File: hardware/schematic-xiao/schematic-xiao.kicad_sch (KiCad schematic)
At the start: 8 parts, among them SW1 SW_STD-ALN, SW2 SW_Push, U4 XIAO ESP32C3

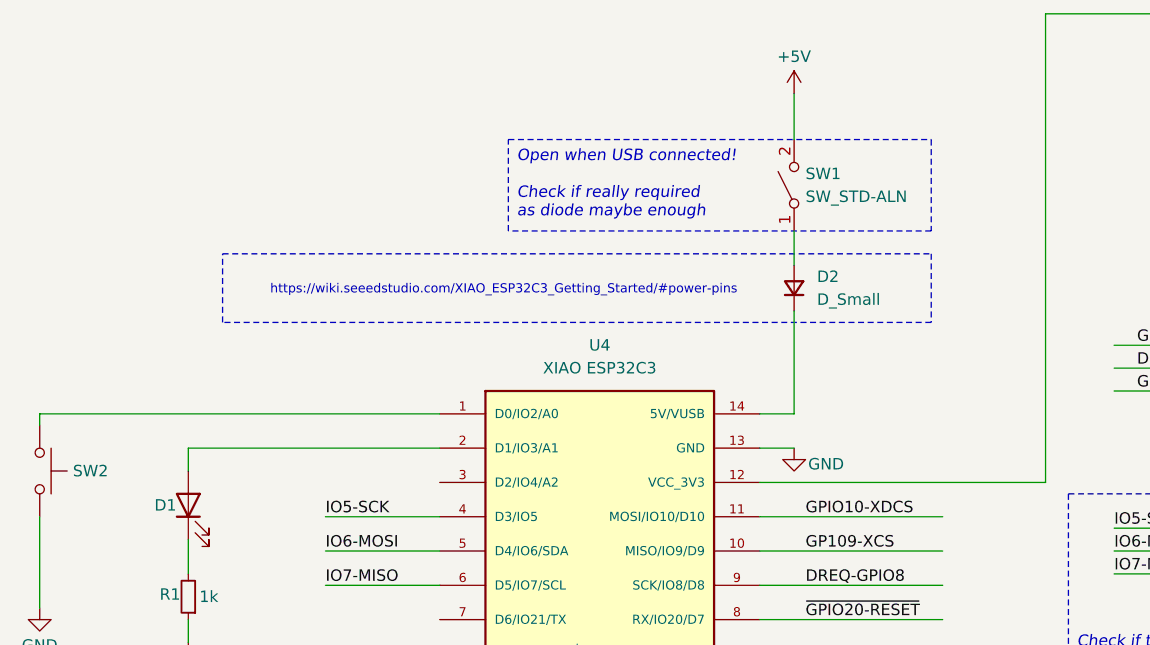
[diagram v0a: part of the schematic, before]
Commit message: New XIAO ESP32C3 schematic
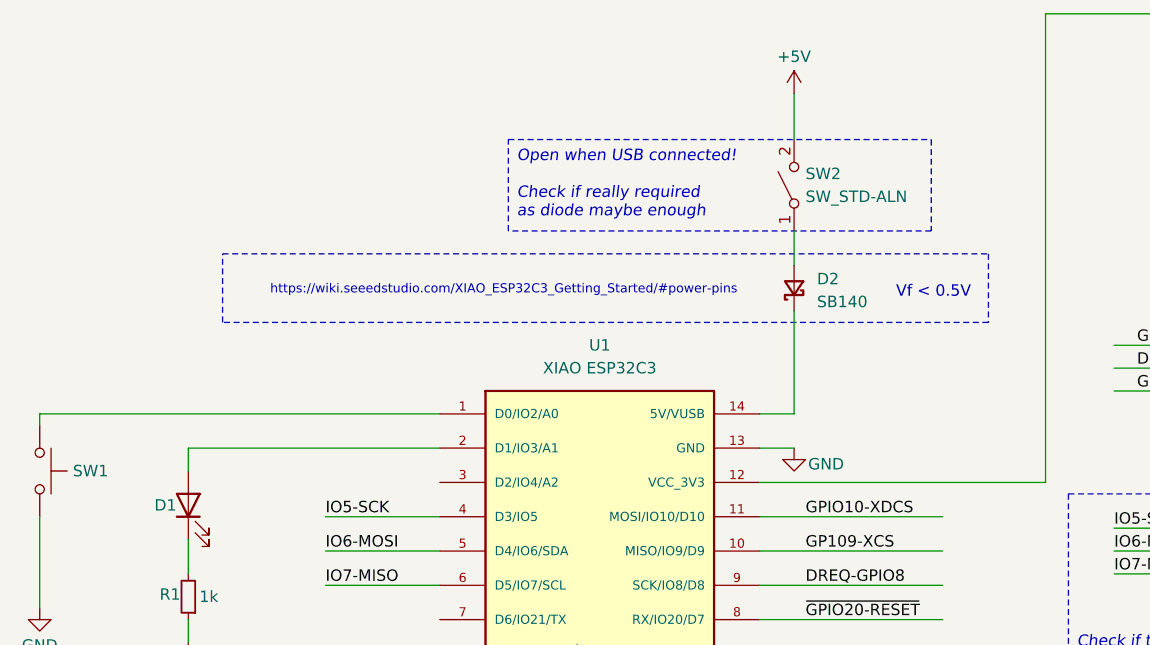
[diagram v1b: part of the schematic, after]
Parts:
- removed D2: D_Small, symbol Device:D_Small
- added D2: SB140, symbol Device:D_Schottky_Small
- renumbered SW2 to SW1, SW1 to SW2, U4 to U1
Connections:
- net at U1.14 (5V/VUSB): now also D2.1 (K)
- net at SW2.1 (A): now also D2.2 (A)
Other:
- note added: "Vf < 0.5V"

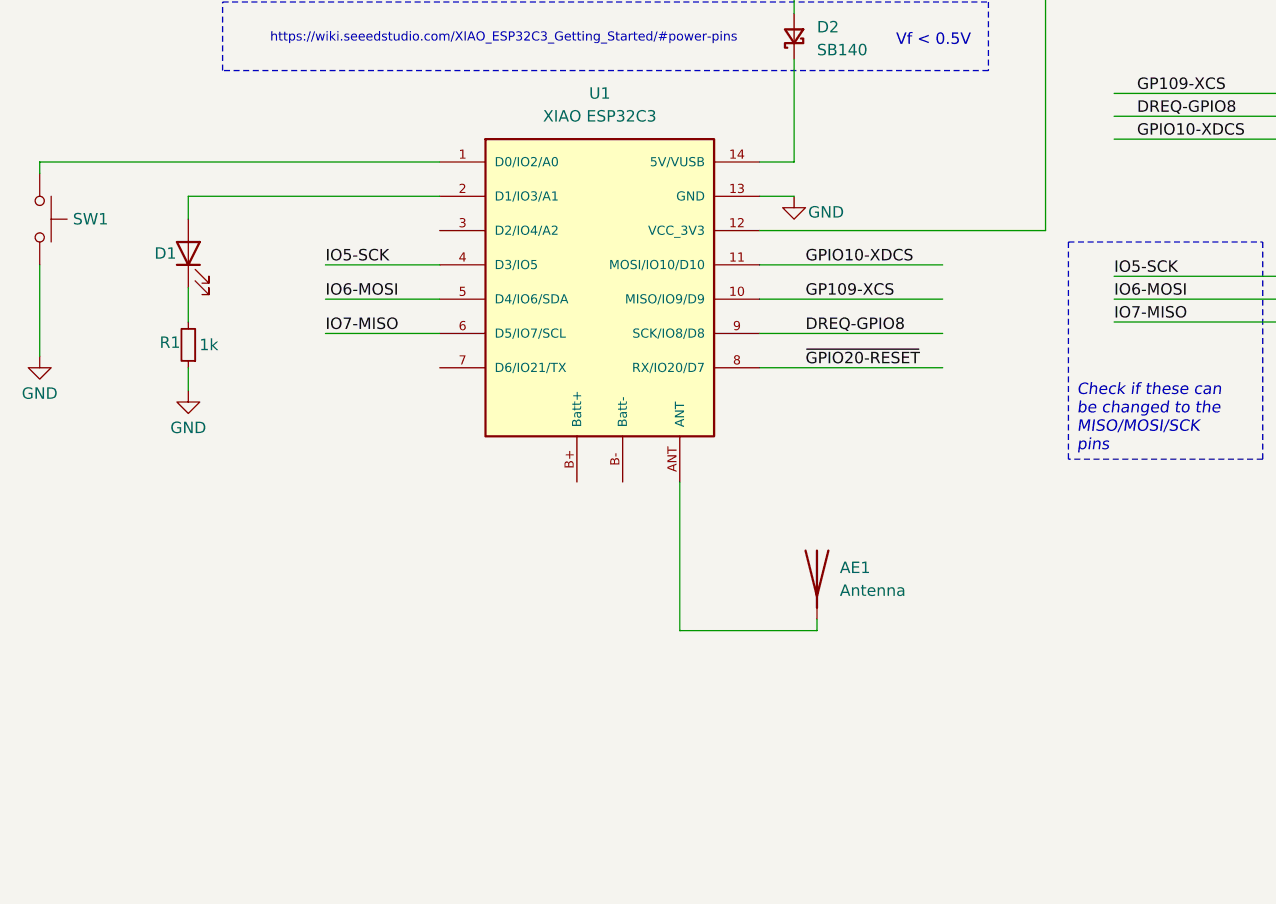
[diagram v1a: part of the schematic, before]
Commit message: Updated schematic to get around XIAO pin restrictions
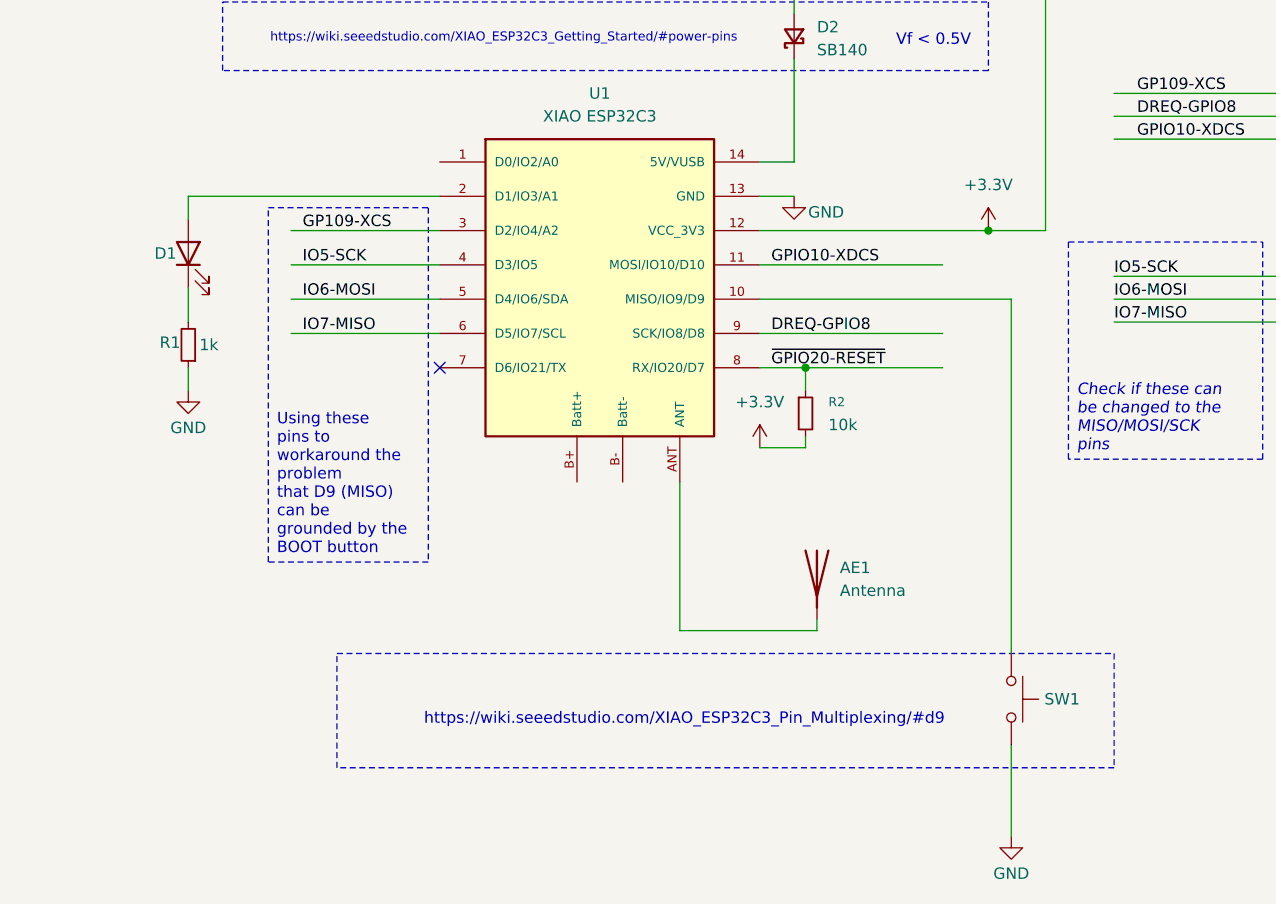
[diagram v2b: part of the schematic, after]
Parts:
- added R2: 10k, symbol Device:R_Small
- U1: Lnk (none) -> https://wiki.seeedstudio.com/XIAO_ESP32C3_Getting_Started/
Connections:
- net GP109-XCS: now also U1.3 (D2/IO4/A2); no longer U1.10 (MISO/IO9/D9)
- net ~{GPIO20-RESET}: now also R2.1
- net +3.3V: now reaches U1.12 (VCC_3V3), U2.2 (3V3)
- net +3.3V: now also R2.2
- net at U1.1 (D0/IO2/A0): no longer SW1.1
- new net: SW1.1, U1.10 (MISO/IO9/D9)
- no-connect marks 1 -> 2
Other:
- note added: "https://wiki.seeedstudio.com/XIAO_ESP32C3_Pin_Multiplexing/#d9"
- moved on the sheet: SW1

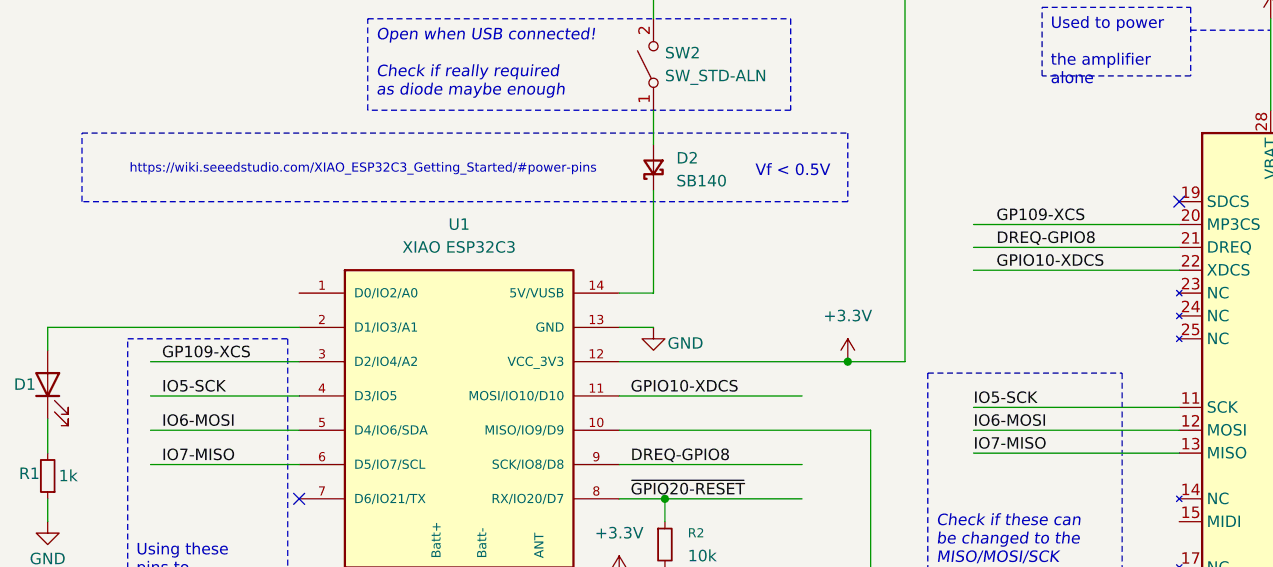
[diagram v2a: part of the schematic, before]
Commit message: perf: optimize WiFi and streaming performance
Hardware:
- Switch target board from ESP32-C3-DevKit-M to Seeed XIAO ESP32C3

WiFi Optimizations:
- Tune WiFi buffer sizes and queue lengths
- Enable AMPDU for both RX and TX
- Set RX/TX queue sizes (20/5)
- Configure dynamic buffer numbers (RX: 16, TX: 16)
- Set RX BA window to 6
- Set max burst size to 8
- MTU configuration has NOT been used

Build Optimizations:
- Add release profile with speed optimization (opt-level = 3)
- Enable LTO for better performance
- Disable debug symbols in release builds
- Configure force-frame-pointers for better debugging support

Dependencies:
- Update esp-hal dependencies to v0.23.1
- Fix esp-alloc dependency to use stable version

Testing:
- Verified WiFi connectivity with new settings
- Tested audio streaming functionality

Documentaion:
- Added CHANGELOG
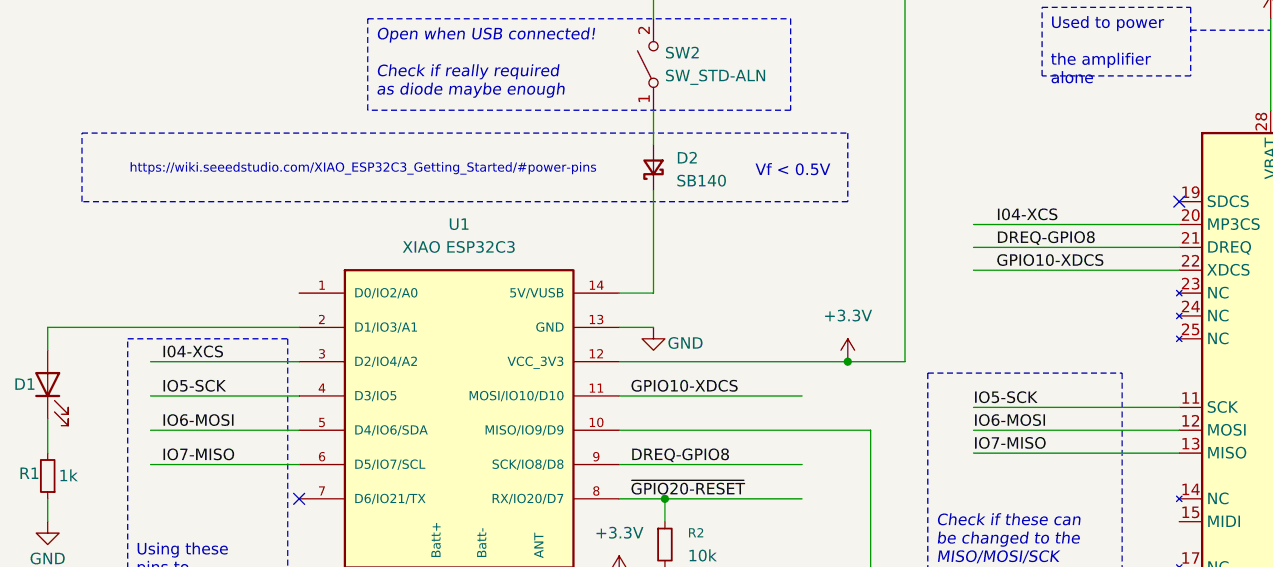
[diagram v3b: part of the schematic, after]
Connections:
- net GP109-XCS renamed I04-XCS
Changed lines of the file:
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@@
 		)
 	)
-	(label "GP109-XCS"
+	(label "I04-XCS"
 		(at 158.75 96.52 0)
 		(effects
@@
 		)
 	)
-	(label "GP109-XCS"
+	(label "I04-XCS"
 		(at 66.04 111.76 0)
 		(effects

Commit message: Protoboard layout
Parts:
- removed SW1: SW_Push, symbol Switch:SW_Push
- removed SW2: SW_STD-ALN, symbol Switch:SW_SPST
- added R3, R4, R5, R6: 10k, symbol Device:R_Small
- added SW1: RotaryEncoder, symbol Device:RotaryEncoder
- added SW2, SW3, SW4, SW5: SW_Push, symbol Switch:SW_Push
- added U3: MCP23S17_SP, Package_DIP:DIP-28_W7.62mm, symbol Interface_Expansion:MCP23S17_SP
- D2: renamed from D1; Field5 (none) -> WIFI Connected
- renumbered D2 to D1, R2 to R1, R1 to R2
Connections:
- net +3.3V: now also R3.1, R4.1, R5.1, R6.1, U3.9 (VDD)
- net +5V: now also D1.2 (A)
- net GND: now also SW1.C, SW2.1, SW3.1, SW4.1, SW5.1, U3.10 (VSS)
- net IO5-SCK: now also U3.12 (SCK)
- net IO6-MOSI: now also U3.13 (SI)
- net IO7-MISO: now also U3.14 (SO)
- net ~{MUX_CS}: now reaches U1.1 (D0/IO2/A0)
- net ~{MUX_CS}: now also U3.11 (~{CS})
- net at D2.2 (A): now also U3.1 (GPB0); no longer U1.2 (D1/IO3/A1)
- new net: R3.2, U3.18 (~{RESET})
- new net: R6.2, U3.15 (A0)
- new net: R5.2, U3.16 (A1)
- new net: R4.2, U3.17 (A2)
- new net: SW1.A, U3.21 (GPA0)
- new net: SW1.B, U3.22 (GPA1)
- new net BTN_1: SW2.2, U3.24 (GPA3)
- new net BTN_2: SW3.2, U3.25 (GPA4)
- new net BTN_3: SW4.2, U3.26 (GPA5)
- new net BTN_4: SW5.2, U3.27 (GPA6)
- new net INTR: U1.2 (D1/IO3/A1)
- new net ~{INTR}: U3.20 (INTA)
- no-connect marks 2 -> 6
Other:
- note added: "This diode allows the XIAO to be powered from USB or PSU. See: https://wiki.seeedstudio.com/XIAO_ESP32C3_Getting_Started/#power-pins"
- note removed: "https://wiki.seeedstudio.com/XIAO_ESP32C3_Getting_Started/#power-pins"
- note removed: "https://wiki.seeedstudio.com/XIAO_ESP32C3_Pin_Multiplexing/#d9"
- moved on the sheet: AE1, D1, D2, R1, R2, U1, U2

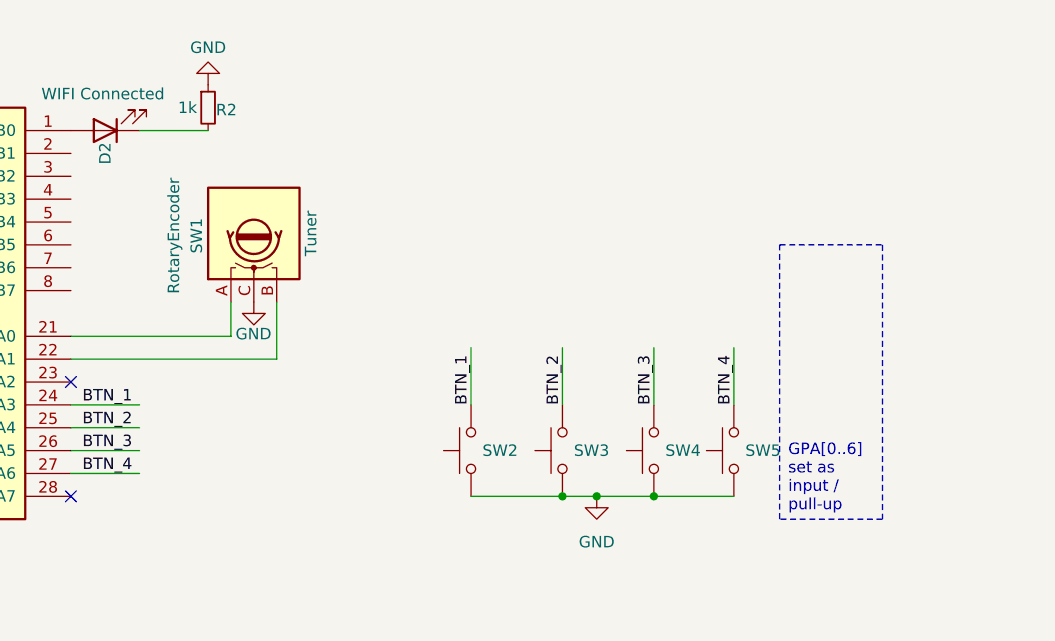
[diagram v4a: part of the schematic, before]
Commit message: Preset buttons work (without interrupt logic)
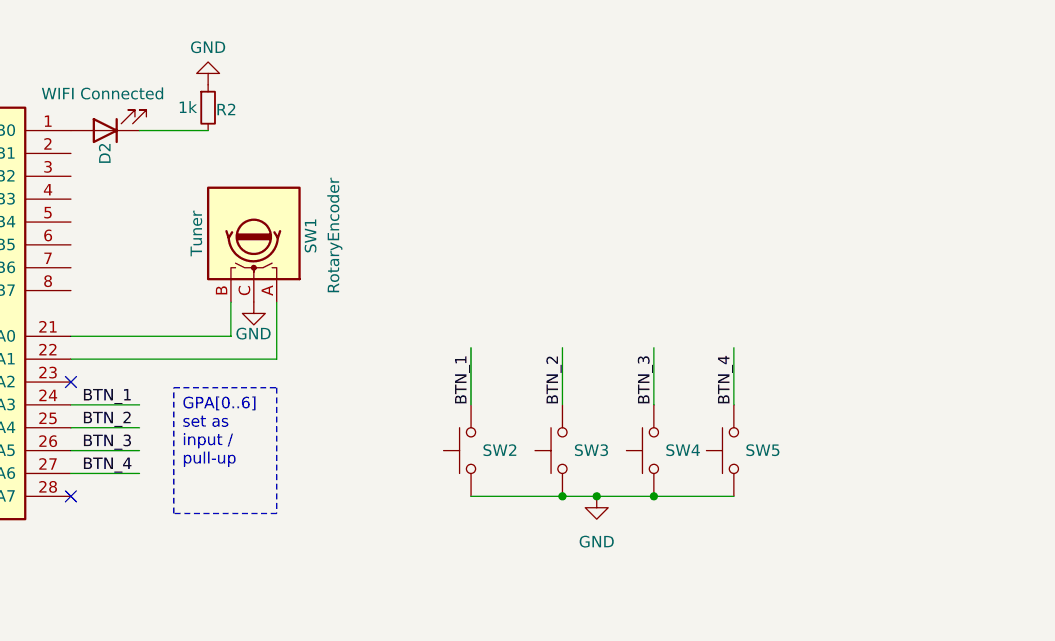
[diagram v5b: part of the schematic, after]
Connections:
- net at U3.21 (GPA0): now also SW1.B; no longer SW1.A
- net at U3.22 (GPA1): now also SW1.A; no longer SW1.B
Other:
- moved on the sheet: SW1
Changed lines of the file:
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@@
 	(text_box "GPA[0..6] set as input / pull-up"
 		(exclude_from_sim no)
-		(at 160.02 156.21 0)
-		(size 11.43 30.48)
+		(at 92.71 172.085 0)
+		(size 11.43 13.97)
 		(margins 0.9525 0.9525 0.9525 0.9525)
 		(stroke
@@
 				(size 1.27 1.27)
 			)
-			(justify left bottom)
+			(justify left top)
 		)
 	)
@@
 	(symbol
 		(lib_id "Device:RotaryEncoder")
-		(at 101.6 154.94 90)
+		(at 101.6 154.94 270)
+		(mirror x)
 		(unit 1)
 		(exclude_from_sim no)
@@
 		(dnp no)
 		(property "Reference" "SW1"
-			(at 95.25 155.194 0)
+			(at 107.95 155.194 0)
 			(effects
 				(font
@@
 		)
 		(property "Value" "RotaryEncoder"
-			(at 92.71 155.194 0)
+			(at 110.49 155.194 0)
 			(effects
 				(font
@@
 		)
 		(property "Footprint" ""
-			(at 97.536 158.75 0)
+			(at 105.664 158.75 0)
 			(effects
 				(font
@@
 		)
 		(property "Datasheet" "~"
-			(at 94.996 154.94 0)
+			(at 108.204 154.94 0)
 			(effects
 				(font
@@
 		)
 		(property "Field5" "Tuner"
-			(at 107.95 154.94 0)
-			(effects
-				(font
+			(at 95.25 154.94 0)
+			(effects
+				(font

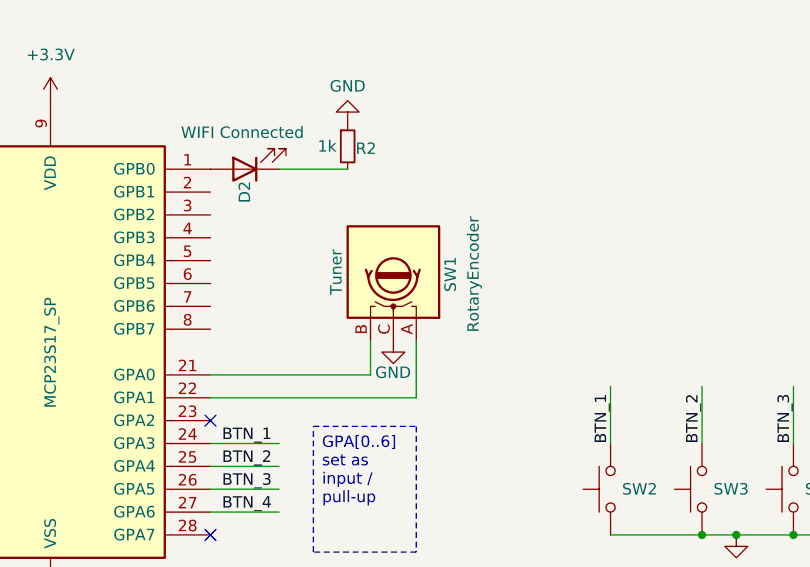
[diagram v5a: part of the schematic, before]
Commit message: Rotary encoder wiring consistent with bitton-board
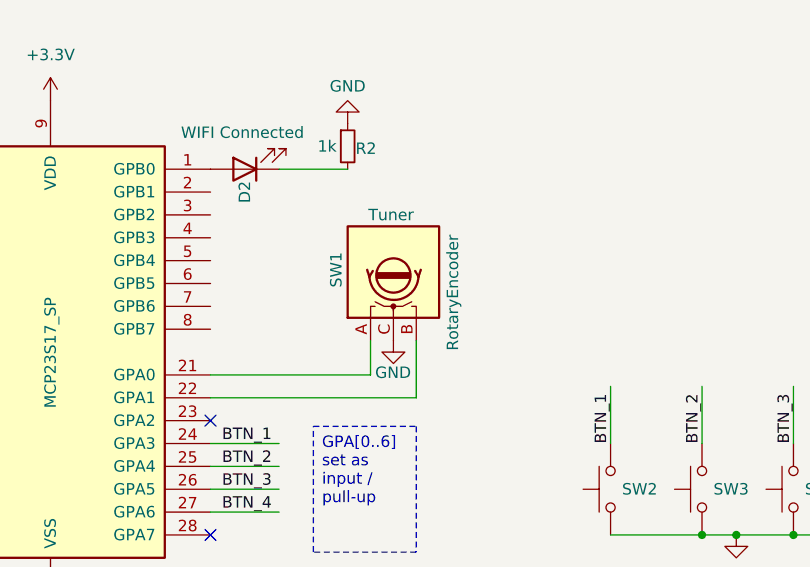
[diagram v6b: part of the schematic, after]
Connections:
- net at U3.21 (GPA0): now also SW1.A; no longer SW1.B
- net at U3.22 (GPA1): now also SW1.B; no longer SW1.A
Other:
- moved on the sheet: SW1
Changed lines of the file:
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@@
 	(symbol
 		(lib_id "Device:RotaryEncoder")
-		(at 101.6 154.94 270)
-		(mirror x)
+		(at 101.6 154.94 90)
 		(unit 1)
 		(exclude_from_sim no)
@@
 		(dnp no)
 		(property "Reference" "SW1"
-			(at 107.95 155.194 0)
+			(at 95.25 154.686 0)
 			(effects
 				(font
@@
 		)
 		(property "Value" "RotaryEncoder"
-			(at 110.49 155.194 0)
+			(at 108.204 157.226 0)
 			(effects
 				(font
@@
 		)
 		(property "Footprint" ""
-			(at 105.664 158.75 0)
+			(at 97.536 158.75 0)
 			(effects
 				(font
@@
 		)
 		(property "Datasheet" "~"
-			(at 108.204 154.94 0)
+			(at 94.996 154.94 0)
 			(effects
 				(font
@@
 		)
 		(property "Field5" "Tuner"
-			(at 95.25 154.94 0)
+			(at 101.346 148.59 90)
 			(effects
 				(font
